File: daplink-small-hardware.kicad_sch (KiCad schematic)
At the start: 46 parts, among them J1 Pin_SWD_FIRMWARE, J2 USB_C_Receptacle_USB2.0, J4 Conn_SWD, J5 Conn_UART, Q1 S8050-SOT23, U1 STM32F103CBTx, U2 RS3236-3.3, Y1 Crystal_GND24

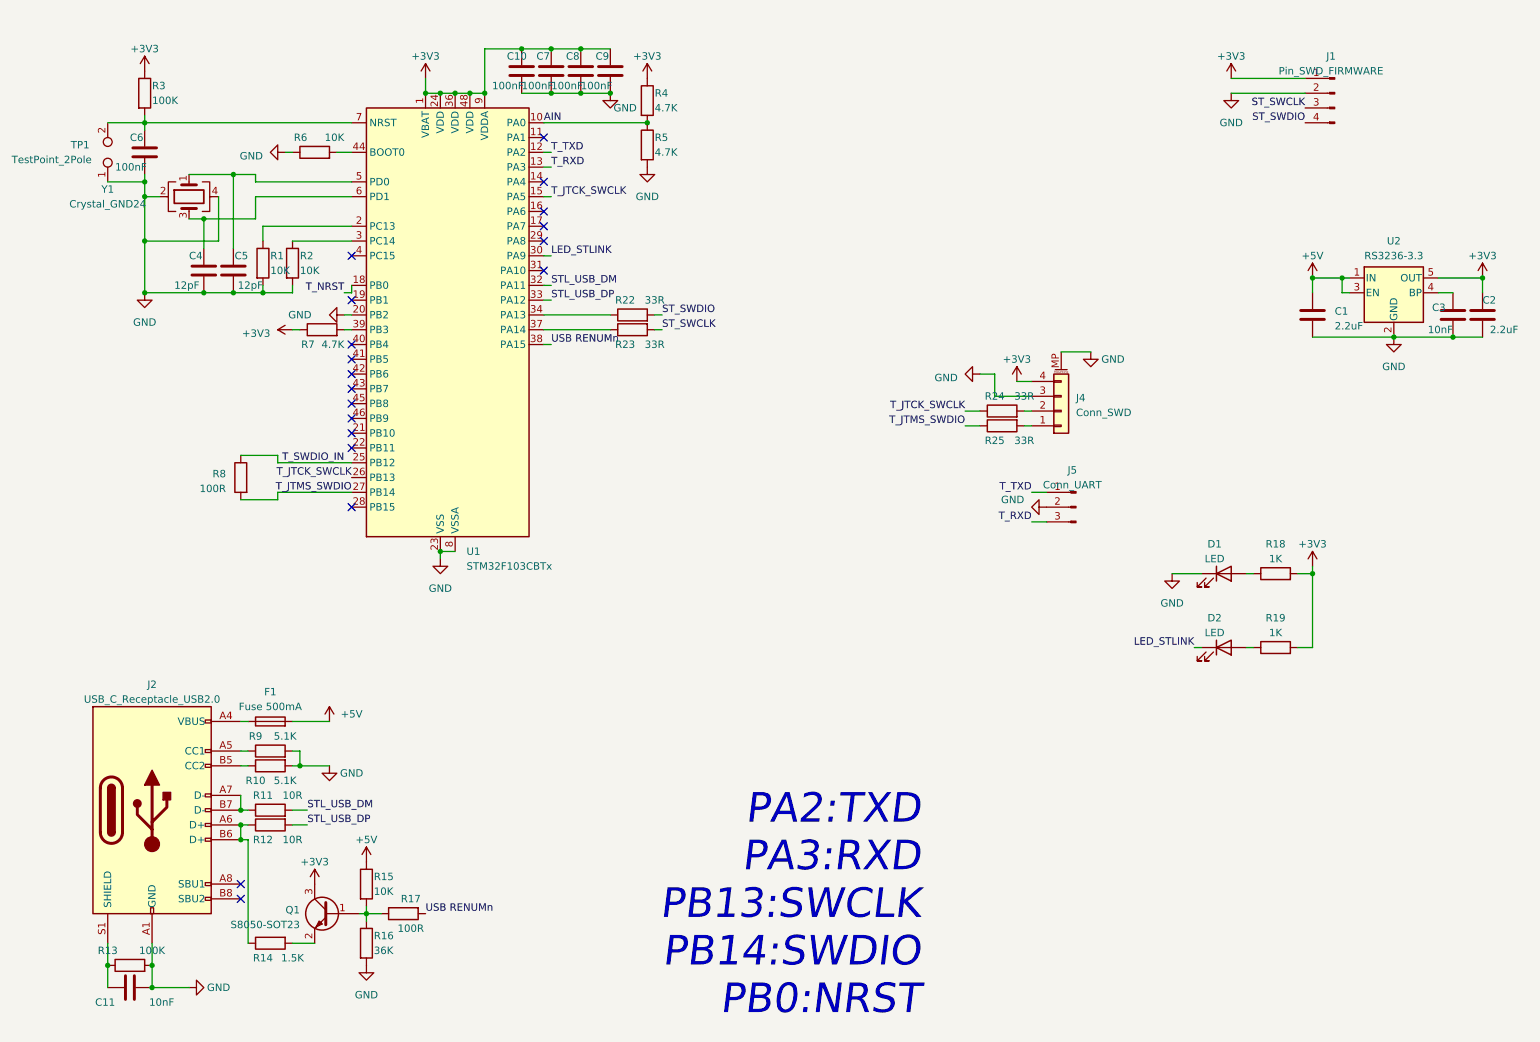
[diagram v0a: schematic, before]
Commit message: Add esd protection; ->Ver1.0.1
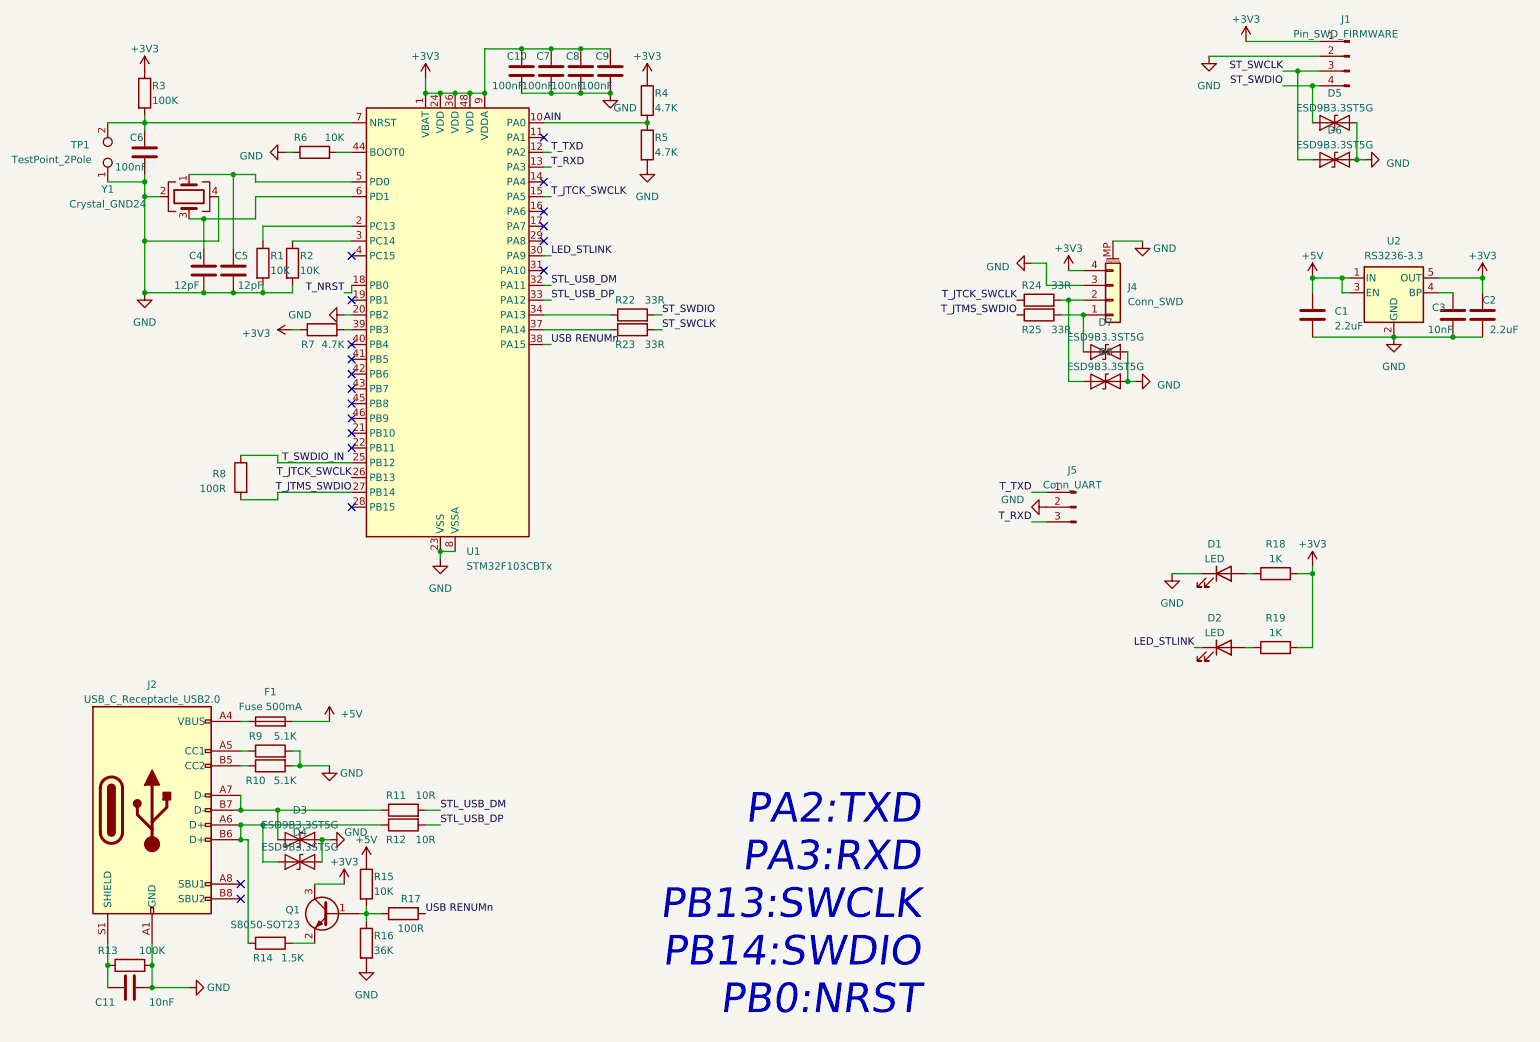
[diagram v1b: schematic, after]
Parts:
- added D3, D4: ESD9B3.3ST5G, Diode_SMD:D_SOD-323, symbol Diode:ESD9B5.0ST5G
- added D5, D6, D7, D8: ESD9B3.3ST5G, Diode_SMD:D_SOD-323, symbol Diode:ESD9B3.3ST5G
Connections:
- net GND: now also D3.2 (A2), D4.2 (A2), D5.2 (A2), D6.2 (A2), D7.2 (A2), D8.2 (A2)
- net ST_SWCLK: now also D6.1 (A1)
- net ST_SWDIO: now also D5.1 (A1)
- net at J2.A6 (D+), J2.B6 (D+), R12.1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: now also D4.1 (A1)
- net at J2.A7 (D-), J2.B7 (D-), R11.1: now also D3.1 (A1)
- net at J4.2 (Pin_2), R24.2: now also D8.1 (A1)
- net at J4.1 (Pin_1), R25.2: now also D7.1 (A1)
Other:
- moved on the sheet: J1, J4, R11, R12, R24, R25
